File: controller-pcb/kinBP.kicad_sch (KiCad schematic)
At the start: 28 parts, among them J1 LEFT_TOP, J10 LEFT_THUMB, J11 RIGHT_THUMB, J12 RIGHT_THUMB, J13 LEFT_THUMB, J2 LEFT_TOP, J3 RIGHT_TOP, J4 RIGHT_TOP, J5 RIGHT_KEYWELL, J6 LEFT_KEYWELL, J7 LEFT_THUMB, J8 RIGHT_THUMB, J9 Conn_02x08_Odd_Even, U1 weact_STM32F4x1

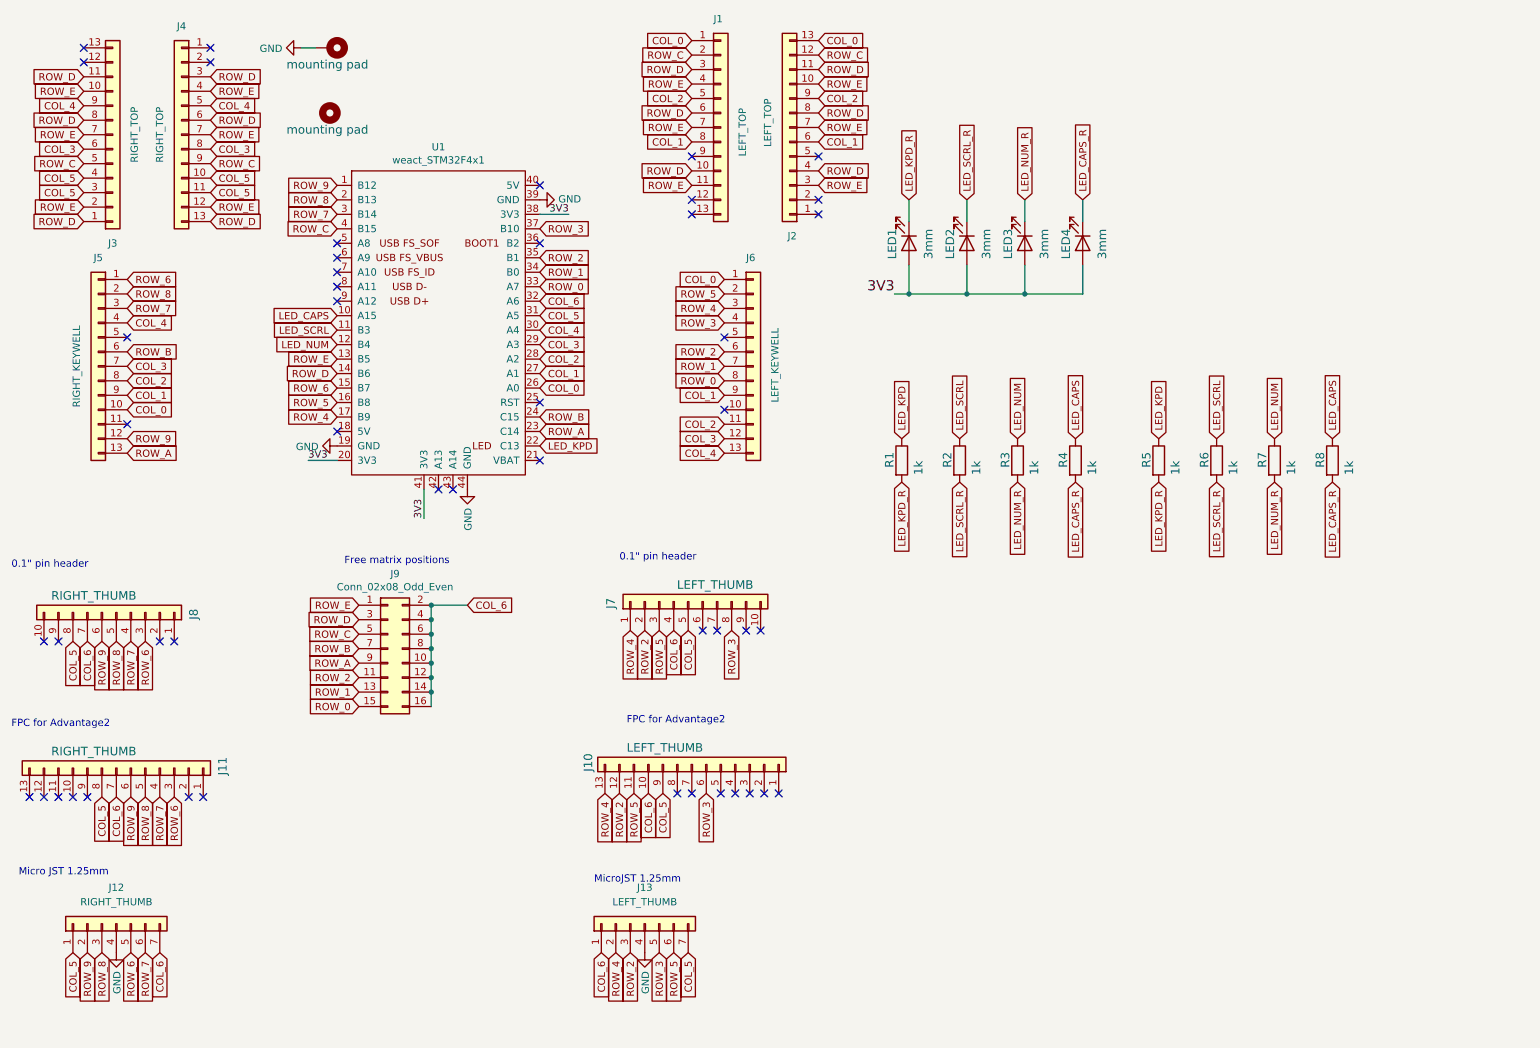
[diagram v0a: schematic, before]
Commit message: River's modified version. Added piezo sounder. Rerouted. Split extra switch header.
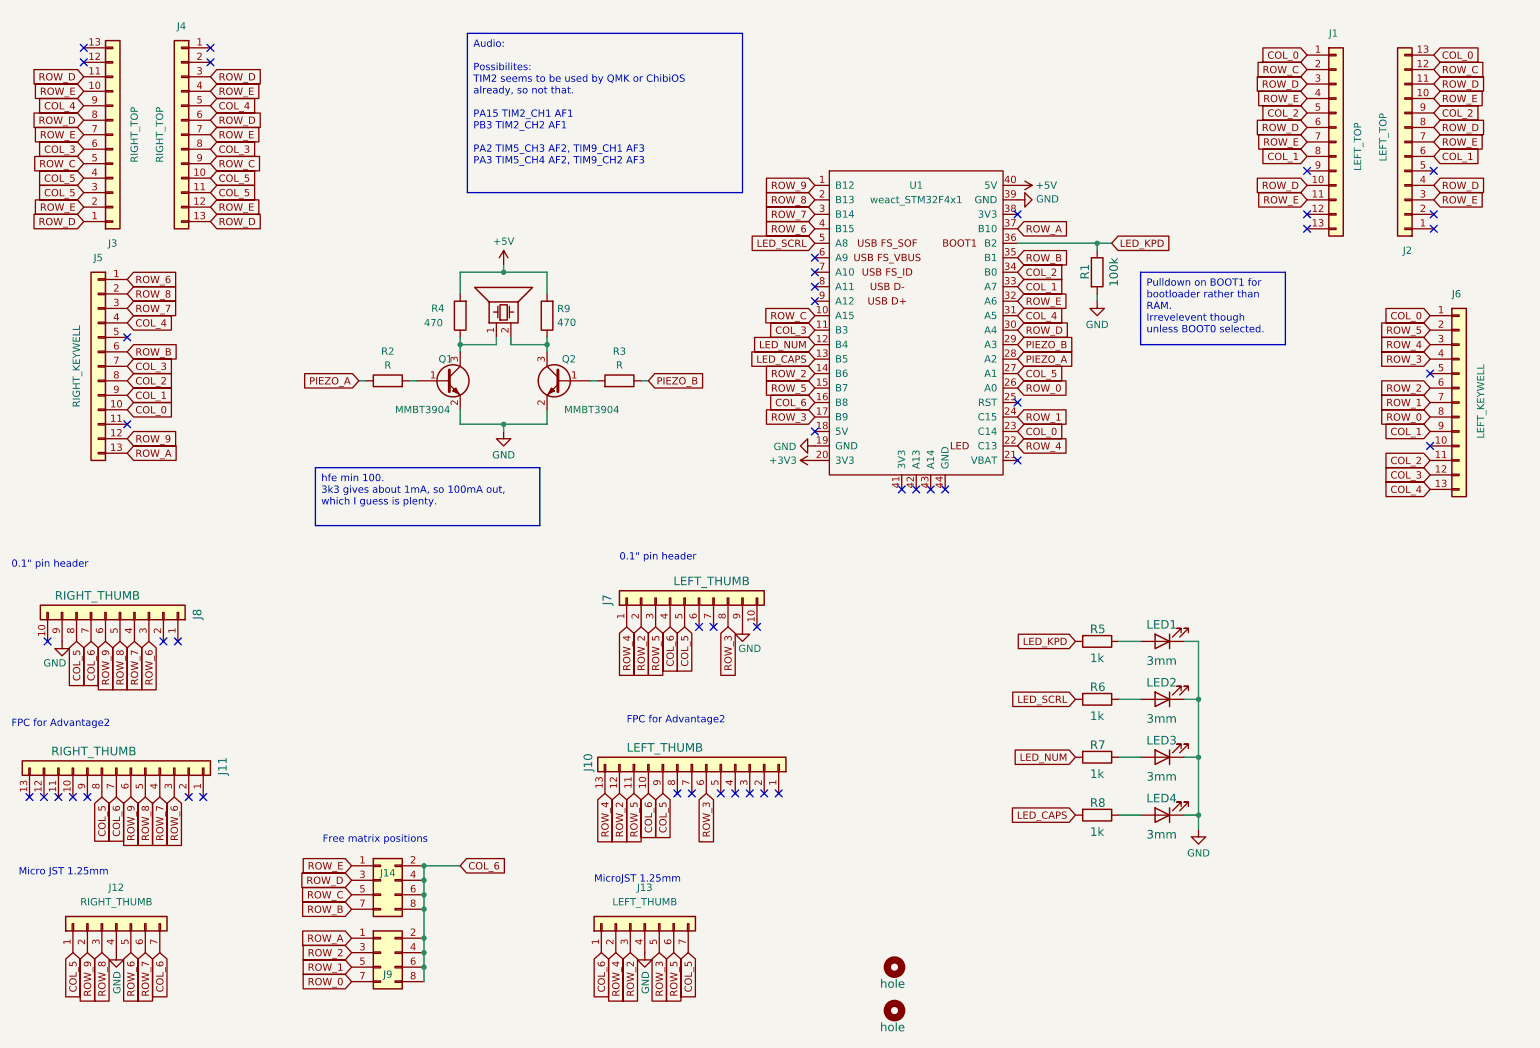
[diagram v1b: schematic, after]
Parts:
- added J14: Conn_02x04_Odd_Even, Connector_PinHeader_2.54mm:PinHeader_2x04_P2.54mm_Vertical, symbol Connector_Generic:Conn_02x04_Odd_Even
- added LS1: Speaker_Crystal, Buzzer_Beeper:MagneticBuzzer_ProSignal_ABT-410-RC, symbol Device:Speaker_Crystal
- added Q1, Q2: MMBT3904, Package_TO_SOT_SMD:SOT-23, symbol Transistor_BJT:MMBT3904
- added R9: 470, Resistor_THT:R_Axial_DIN0207_L6.3mm_D2.5mm_P7.62mm_Horizontal, symbol Device:R
- H1: value mounting pad -> hole; footprint MountingHole:MountingHole_4.3mm_M4_Pad -> MountingHole:MountingHole_4.3mm_M4; symbol Mechanical:MountingHole_Pad -> Mechanical:MountingHole
- H2: value mounting pad -> hole
- J9: value Conn_02x08_Odd_Even -> Conn_02x04_Odd_Even; footprint Connector_PinHeader_2.54mm:PinHeader_2x08_P2.54mm_Vertical -> Connector_PinHeader_2.54mm:PinHeader_2x04_P2.54mm_Vertical; symbol Connector_Generic:Conn_02x08_Odd_Even -> Connector_Generic:Conn_02x04_Odd_Even
- LED1, LED2, LED3, LED4: footprint LED_THT:LED_D3.0mm -> keyboards:LED_D3.0mm_centered
- R1: value 1k -> 100k; footprint Resistor_SMD:R_0805_2012Metric_Pad1.20x1.40mm_HandSolder -> Resistor_THT:R_Axial_DIN0207_L6.3mm_D2.5mm_P7.62mm_Horizontal
- R2, R3: value 1k -> R; footprint Resistor_SMD:R_0805_2012Metric_Pad1.20x1.40mm_HandSolder -> Resistor_THT:R_Axial_DIN0207_L6.3mm_D2.5mm_P7.62mm_Horizontal
- R4: value 1k -> 470; footprint Resistor_SMD:R_0805_2012Metric_Pad1.20x1.40mm_HandSolder -> Resistor_THT:R_Axial_DIN0207_L6.3mm_D2.5mm_P7.62mm_Horizontal
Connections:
- net COL_0: now also U1.23 (C14); no longer U1.26 (A0)
- net COL_1: now also U1.33 (A7); no longer U1.27 (A1)
- net COL_2: now also U1.34 (B0); no longer U1.28 (A2)
- net COL_3: now also U1.11 (B3); no longer U1.29 (A3)
- net COL_4: now also U1.31 (A5); no longer U1.30 (A4)
- net COL_5: now also U1.27 (A1); no longer U1.31 (A5)
- net COL_6: now also U1.16 (B8), J14.2 (Pin_2), J14.4 (Pin_4), J14.6 (Pin_6), J14.8 (Pin_8); no longer J9.10 (Pin_10), J9.12 (Pin_12), J9.14 (Pin_14), J9.16 (Pin_16), U1.32 (A6)
- net GND: now also J7.9 (Pin_9), J8.9 (Pin_9), LED1.1 (K), LED2.1 (K), LED3.1 (K), LED4.1 (K), R1.2, Q1.2 (E), Q2.2 (E); no longer H1.1, U1.44 (GND)
- net LED_CAPS: now also R8.2, U1.13 (B5); no longer R4.1, R8.1, U1.10 (A15)
- net LED_KPD: now also R5.2, U1.36 (B2); no longer R5.1, U1.22 (C13)
- net LED_NUM: now also R7.2; no longer R3.1, R7.1
- net LED_SCRL: now also R6.2, U1.5 (A8); no longer R2.1, R6.1, U1.11 (B3)
- net ROW_0: now also J9.7 (Pin_7), U1.26 (A0); no longer J9.15 (Pin_15), U1.33 (A7)
- net ROW_1: now also J9.5 (Pin_5), U1.24 (C15); no longer J9.13 (Pin_13), U1.34 (B0)
- net ROW_2: now also J9.3 (Pin_3), U1.14 (B6); no longer J9.11 (Pin_11), U1.35 (B1)
- net ROW_3: now also U1.17 (B9); no longer U1.37 (B10)
- net ROW_4: now also U1.22 (C13); no longer U1.17 (B9)
- net ROW_5: now also U1.15 (B7); no longer U1.16 (B8)
- net ROW_6: now also U1.4 (B15); no longer U1.15 (B7)
- net ROW_A: now also J9.1 (Pin_1), U1.37 (B10); no longer J9.9 (Pin_9), U1.23 (C14)
- net ROW_B: now also U1.35 (B1), J14.7 (Pin_7); no longer J9.7 (Pin_7), U1.24 (C15)
- net ROW_C: now also U1.10 (A15), J14.5 (Pin_5); no longer J9.5 (Pin_5), U1.4 (B15)
- net ROW_D: now also U1.30 (A4), J14.3 (Pin_3); no longer J9.3 (Pin_3), U1.14 (B6)
- net ROW_E: now also U1.32 (A6), J14.1 (Pin_1); no longer J9.1 (Pin_1), U1.13 (B5)
- net +5V: now reaches U1.40 (5V)
- net +5V: now also R4.2, R9.2
- removed net 3V3: LED1.2 (A), LED2.2 (A), LED3.2 (A), LED4.2 (A), U1.20 (3V3), U1.38 (3V3), U1.41 (3V3)
- removed net LED_CAPS_R: LED4.1 (K), R4.2, R8.2
- removed net LED_KPD_R: LED1.1 (K), R1.2, R5.2
- removed net LED_NUM_R: LED3.1 (K), R3.2, R7.2
- removed net LED_SCRL_R: LED2.1 (K), R2.2, R6.2
- new net: LED1.2 (A), R5.1
- new net: LED2.2 (A), R6.1
- new net: LED3.2 (A), R7.1
- new net: LED4.2 (A), R8.1
- new net: LS1.1, Q1.3 (C), R4.1
- new net: LS1.2, Q2.3 (C), R9.1
- new net: Q2.1 (B), R3.2
- new net: Q1.1 (B), R2.2
- new net +3V3: U1.20 (3V3)
- new net PIEZO_A: R2.1, U1.28 (A2)
- new net PIEZO_B: R3.1, U1.29 (A3)
- no-connect marks 48 -> 46
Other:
- company: Dmitriy Nosachev -> River Cat
- moved on the sheet: J1, J2, J6, J7, J8, LED1, LED2, LED3, LED4, R5, R6, R7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

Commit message: Added connector for original external USB / footpedal cable. Fixed LED positions. Prob other stuff I forgot.
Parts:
- removed R1: 100k, Resistor_THT:R_Axial_DIN0207_L6.3mm_D2.5mm_P7.62mm_Horizontal, symbol Device:R
- added J15: USB Cable Socket, Connector_JST:JST_PH_B7B-PH-K_1x07_P2.00mm_Vertical, symbol Connector:Conn_01x07_Socket
- H1: footprint MountingHole:MountingHole_4.3mm_M4 -> river:MountingHole_4.3mm_M4_No_Copper
- J7, J8: footprint Connector_PinHeader_2.54mm:PinHeader_1x10_P2.54mm_Vertical -> Connector_PinHeader_2.54mm:PinHeader_1x09_P2.54mm_Vertical; symbol Connector_Generic:Conn_01x10 -> Connector_Generic:Conn_01x09
- LS1: value Speaker_Crystal -> LD-BZEN-1205LOUDITY; footprint Buzzer_Beeper:MagneticBuzzer_ProSignal_ABT-410-RC -> river:Piezos_12mm
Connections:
- net +5V: now also J15.3 (Pin_3)
- net COL_6: now also J15.2 (Pin_2)
- net GND: now also J15.6 (Pin_6)
- net ROW_A: now also J15.7 (Pin_7)
- net ROW_B: now also J15.1 (Pin_1)
- net USB_D-: now reaches U1.8 (A11)
- net USB_D-: now also J15.4 (Pin_4)
- net USB_D+: now reaches U1.9 (A12)
- net USB_D+: now also J15.5 (Pin_5)
- no-connect marks 46 -> 42

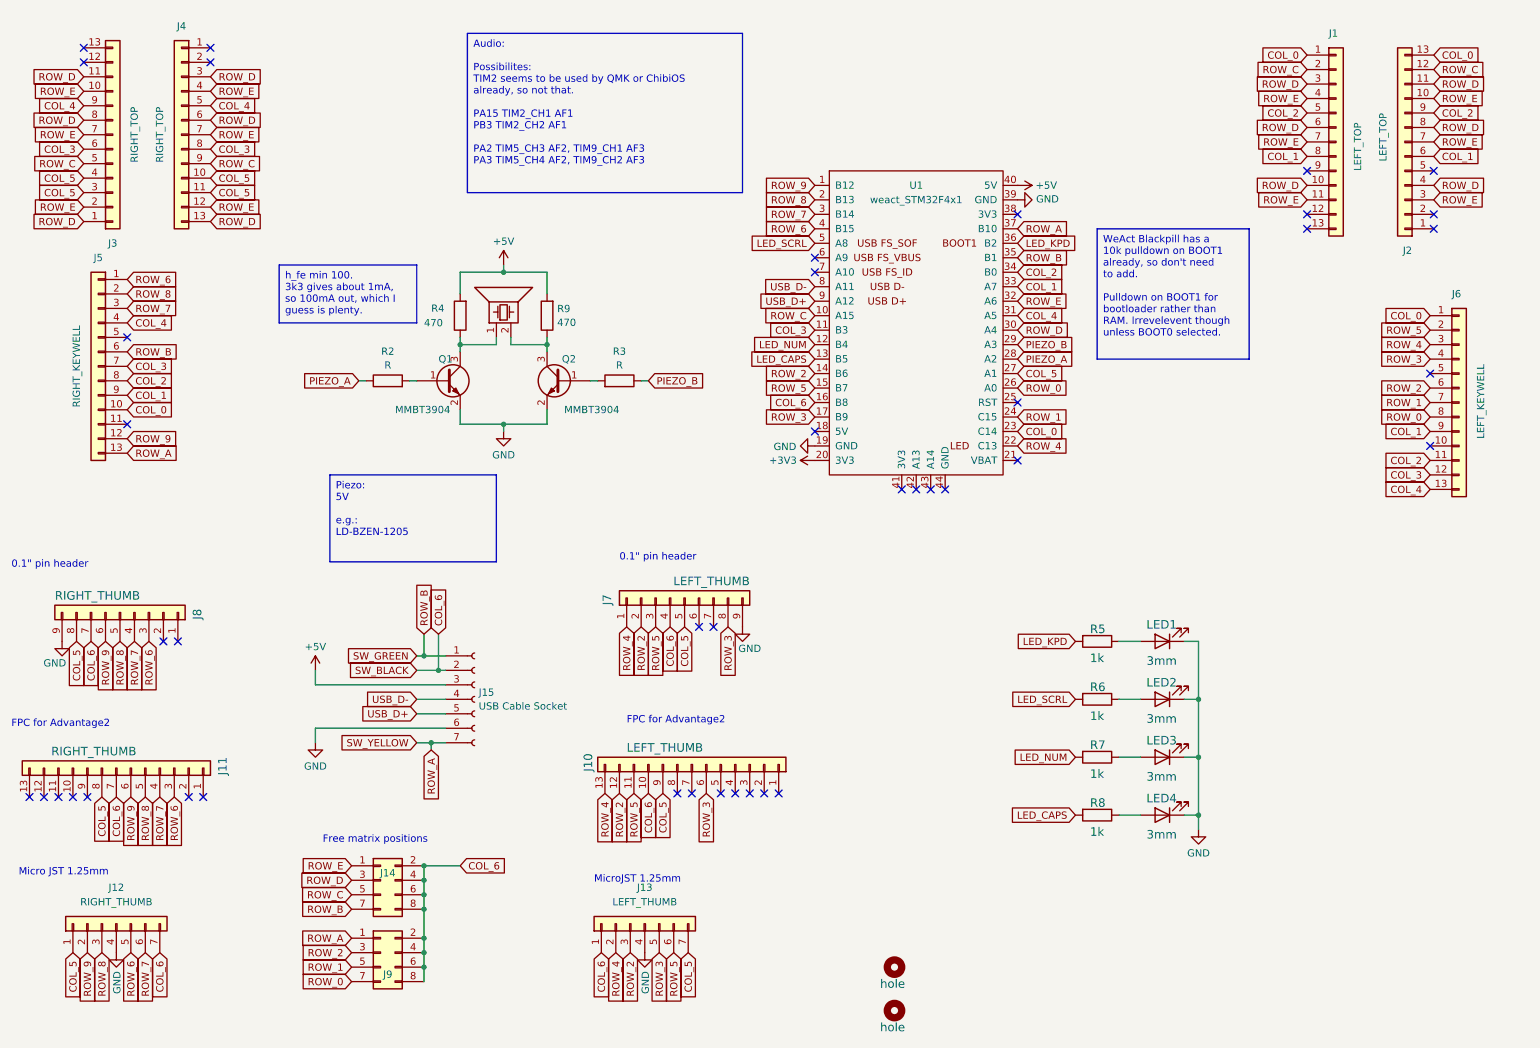
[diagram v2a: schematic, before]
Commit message: V0.2 as made, except then shifted screw hole down 0.2mm.
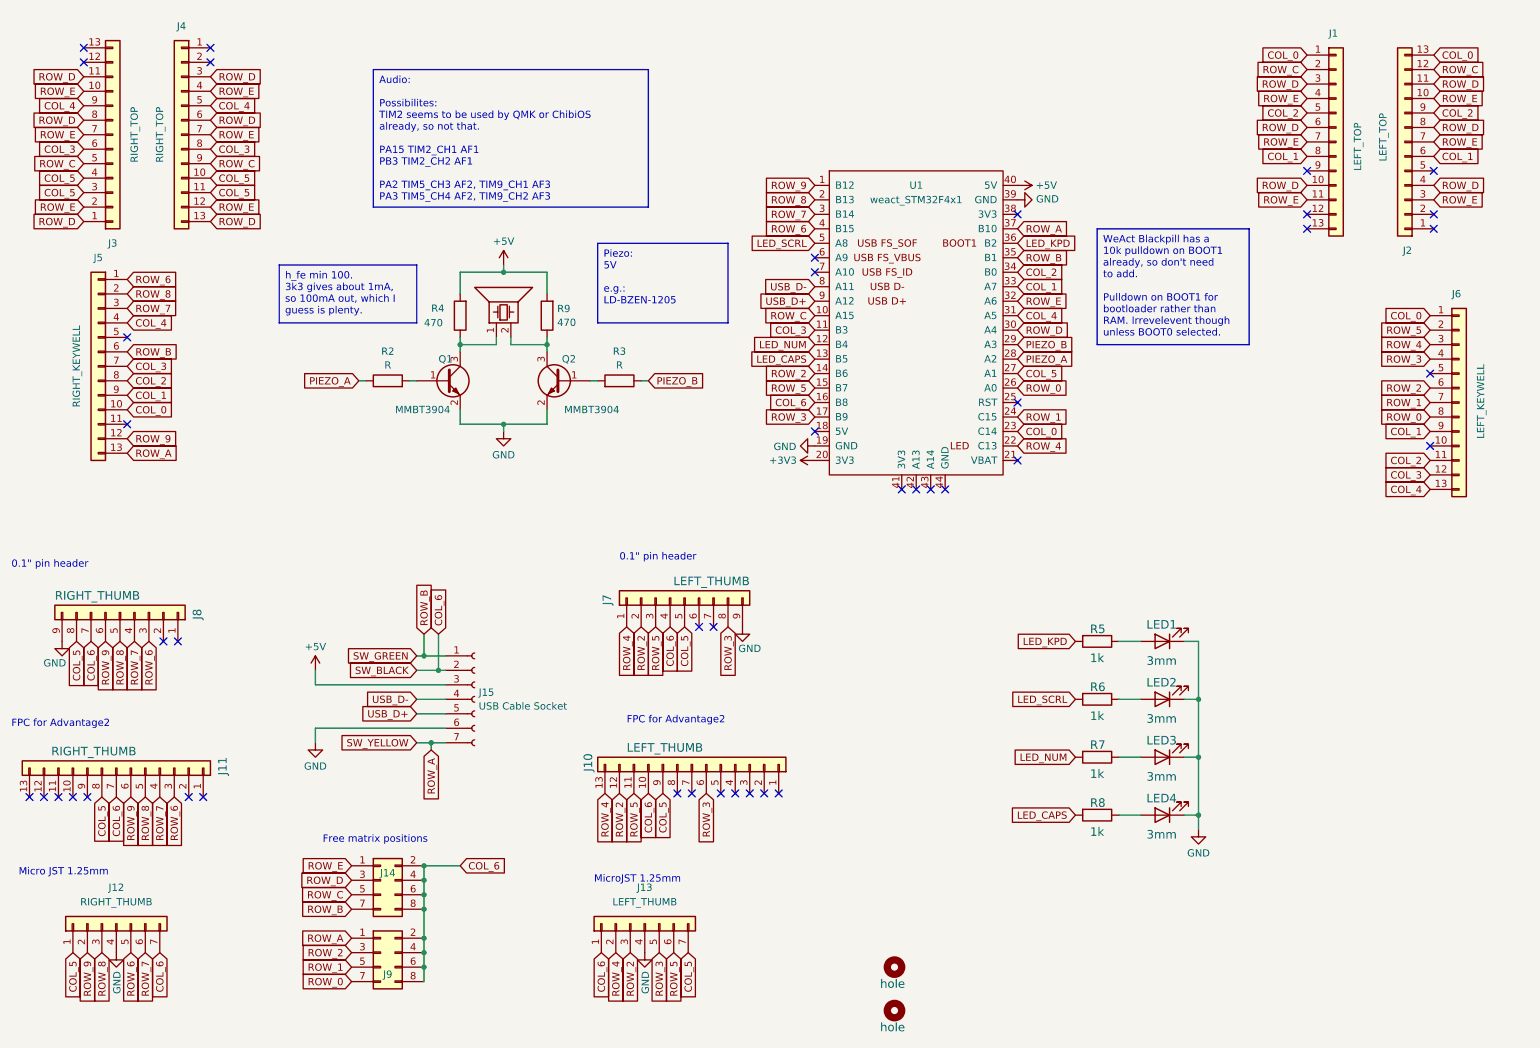
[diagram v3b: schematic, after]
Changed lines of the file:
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@@
 	(text_box "Piezo:\n5V\n\ne.g.:\nLD-BZEN-1205"
 		(exclude_from_sim no)
-		(at 69.85 93.98 0)
-		(size 29.21 15.24)
+		(at 116.84 53.34 0)
+		(size 22.86 13.97)
 		(stroke
 			(width 0)
@@
 		(exclude_from_sim no)
 		(at 204.47 50.8 0)
-		(size 26.67 22.86)
+		(size 26.67 20.32)
 		(stroke
 			(width 0)
@@
 	(text_box "Audio:\n\nPossibilites:\nTIM2 seems to be used by QMK or ChibiOS already, so not that.\n\nPA15 TIM2_CH1 AF1\nPB3 TIM2_CH2 AF1\n\nPA2 TIM5_CH3 AF2, TIM9_CH1 AF3\nPA3 TIM5_CH4 AF2, TIM9_CH2 AF3"
 		(exclude_from_sim no)
-		(at 93.98 16.51 0)
-		(size 48.26 27.94)
+		(at 77.47 22.86 0)
+		(size 48.26 24.13)
 		(stroke
 			(width 0)

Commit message: Bumped version to V0.3. Added some notes, metadata.
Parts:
- R2, R3: value R -> 3k3
- R5, R6, R7, R8: Note (none) -> Modify value for chosen LEDs.
- U1: Note (none) -> Weact Blackpill devboard.
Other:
- title: kinBP keyboard controller -> River's Blackpill Kinesis Advantage Controller
